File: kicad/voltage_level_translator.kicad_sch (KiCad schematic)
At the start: 21 parts, among them Q1 2N7002, SW1 TA-3532S-A2, U3 TS5A3157DBVR, U4 TXS0108EPW, U5 TXS0108EPW, U6 TMUX1574PW, U7 TMUX1574PW

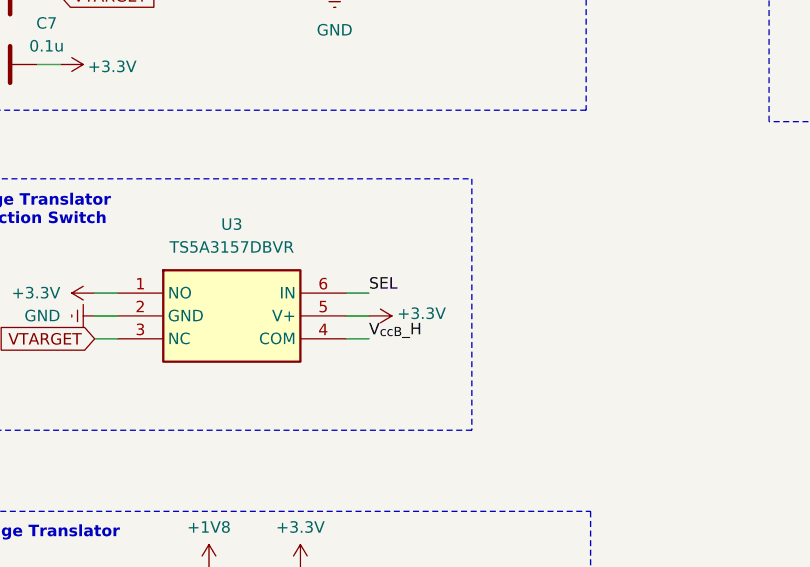
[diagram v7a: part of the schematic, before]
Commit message: TS5A3157 SEL fixed
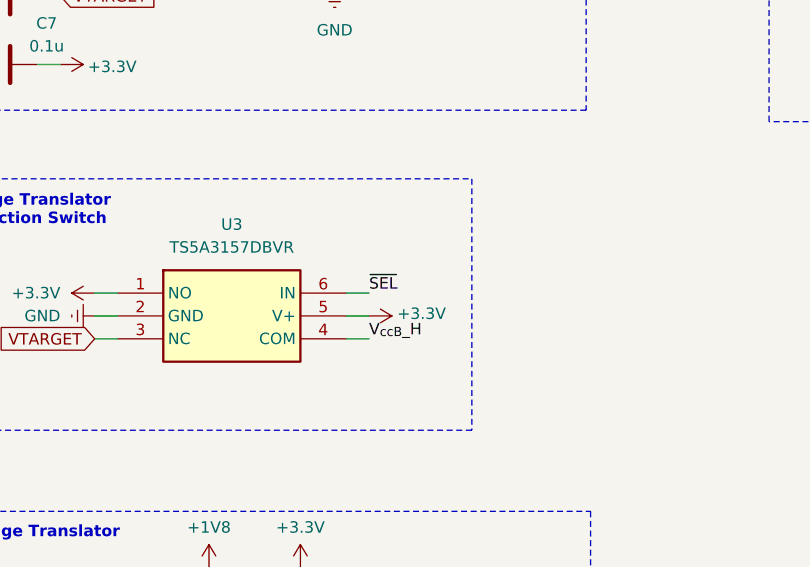
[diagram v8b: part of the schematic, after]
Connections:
- net SEL: no longer U3.6 (IN)
- net ~{SEL}: now also U3.6 (IN)
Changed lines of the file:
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@@
-		)
-	)
-	(label "SEL"
-		(at 71.12 102.87 0)
-		(effects
-			(font
-				(size 1.27 1.27)
-			)
-			(justify left bottom)
 		)
 	)
@@
 		)
 	)
+	(label "~{SEL}"
+		(at 71.12 102.87 0)
+		(effects
+			(font
+				(size 1.27 1.27)
+			)
+			(justify left bottom)
+		)
+	)
